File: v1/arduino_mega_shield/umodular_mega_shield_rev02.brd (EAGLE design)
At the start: 53.5 x 100 mm, 31 parts, among them IC1 23LC1024, IC2 74HC4050/CD4050, IC3 6N138, U1 ARDUINO-MEGA-SHIELD

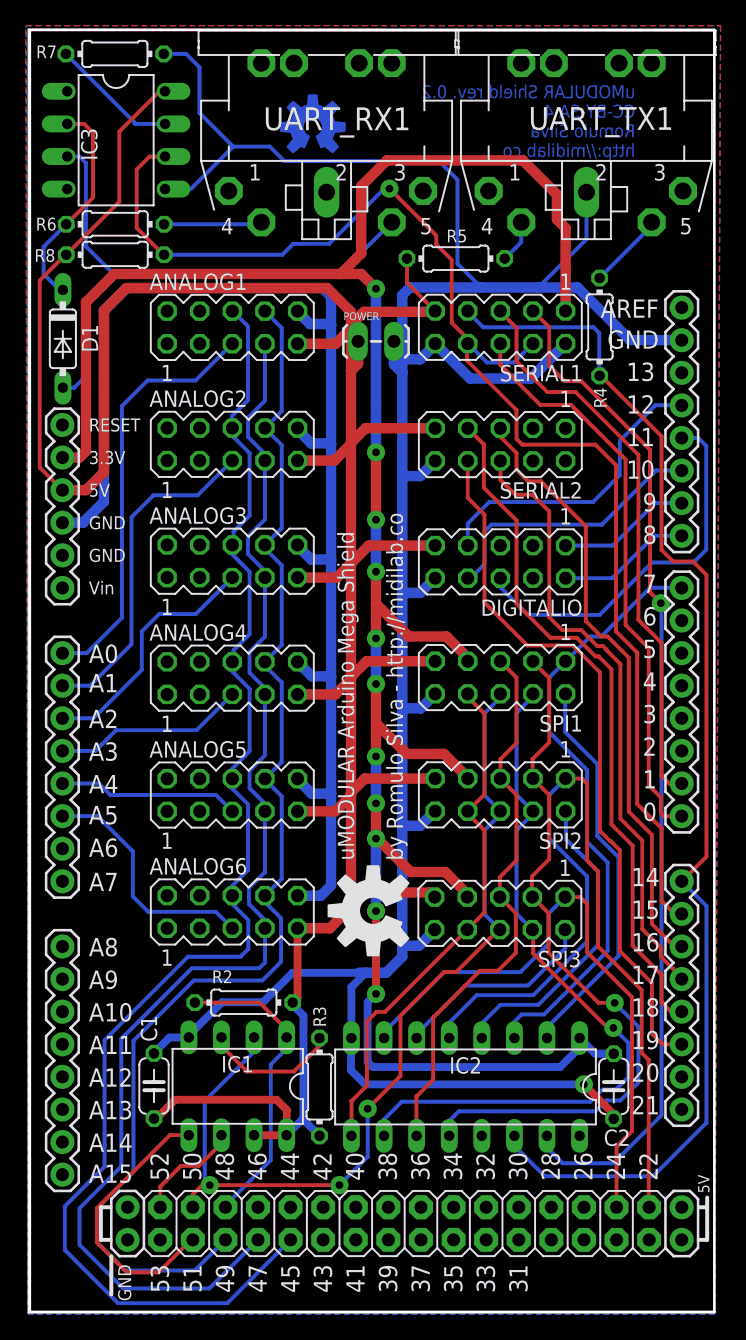
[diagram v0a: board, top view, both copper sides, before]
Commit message: revert arduino mega shiled back to make use of SPI on shared subsystem
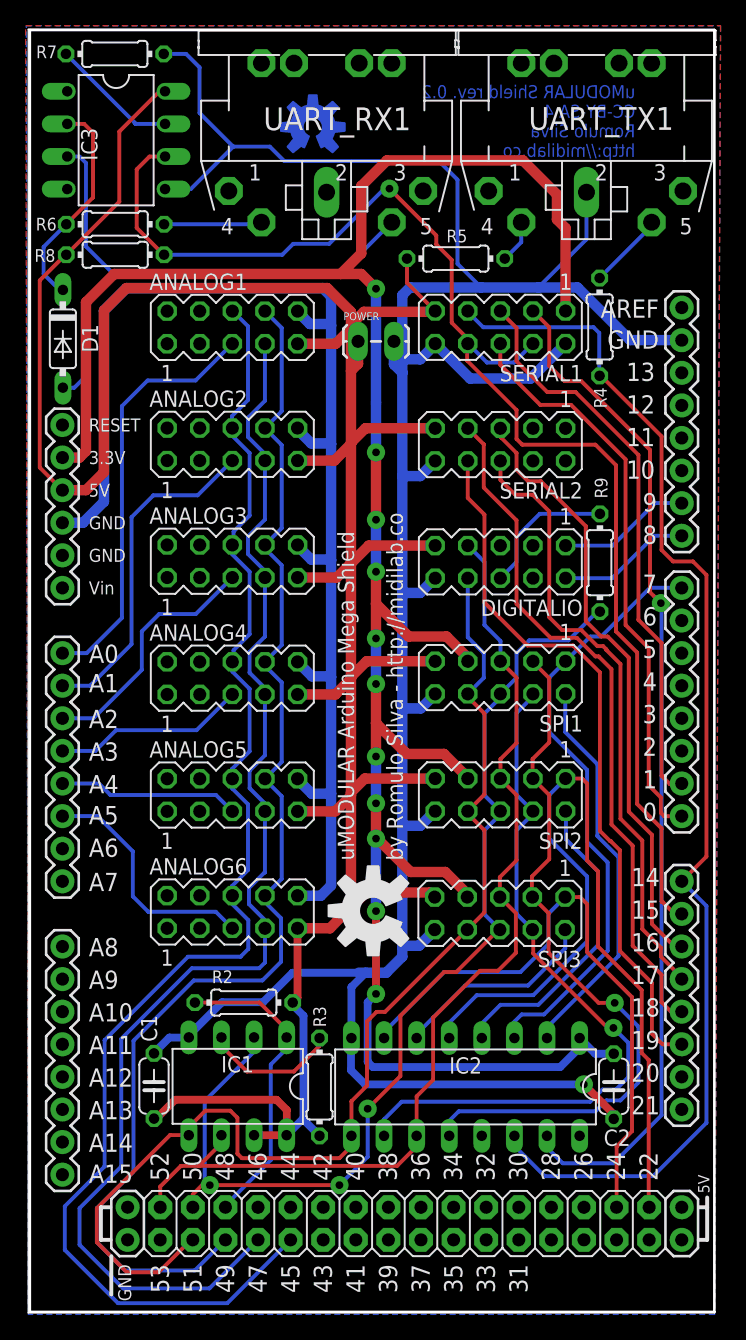
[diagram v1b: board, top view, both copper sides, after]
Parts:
- added R9: 2.2k, rcl:0204/7@1
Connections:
- net LATCH_165 renamed SPI_SS5
- net LATCH_595 renamed SPI_SS4
- removed net SDCARD_CLOCK: IC2.11, U1.39
- removed net SDCARD_MISO: SPI1.6, U1.40
- removed net SDCARD_MOSI: IC2.9, U1.38
- removed net SR_CLOCK: DIGITALIO.7, U1.12
- removed net SR_DATA_165: DIGITALIO.6, U1.11
- removed net SR_DATA_595: DIGITALIO.8, U1.10
- new net N$9: DIGITALIO.6, R9.2
- net SPI_CLOCK: now also DIGITALIO.7, IC2.11
- net SPI_MISO: now also R9.1, SPI1.6
- net SPI_MOSI: now also DIGITALIO.8, IC2.9
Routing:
- net SR_DATA_165: track 30.0 -> 0.00 mm
- net SPI_CLOCK: track 52.9 -> 80.5 mm
- net SPI_MOSI: track 63.2 -> 90.7 mm
- net SR_CLOCK: track 23.8 -> 0.00 mm
- net SR_DATA_595: track 21.7 -> 0.00 mm
- net SPI_MISO: track 71.8 -> 83.6 mm
- net N$9: track 0.00 -> 11.0 mm
